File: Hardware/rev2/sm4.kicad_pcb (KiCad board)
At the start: 4 copper layers, 65 x 56 mm, 133 parts, among them J1 Motor1, J10 CAN bus, J2 Termination, J3 CAN bus, J4 Motor1, J5 I2C, J6 Power, J7 USB_C_Receptacle_USB2.0, J8 Conn_01x05_Male, J9 I2C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

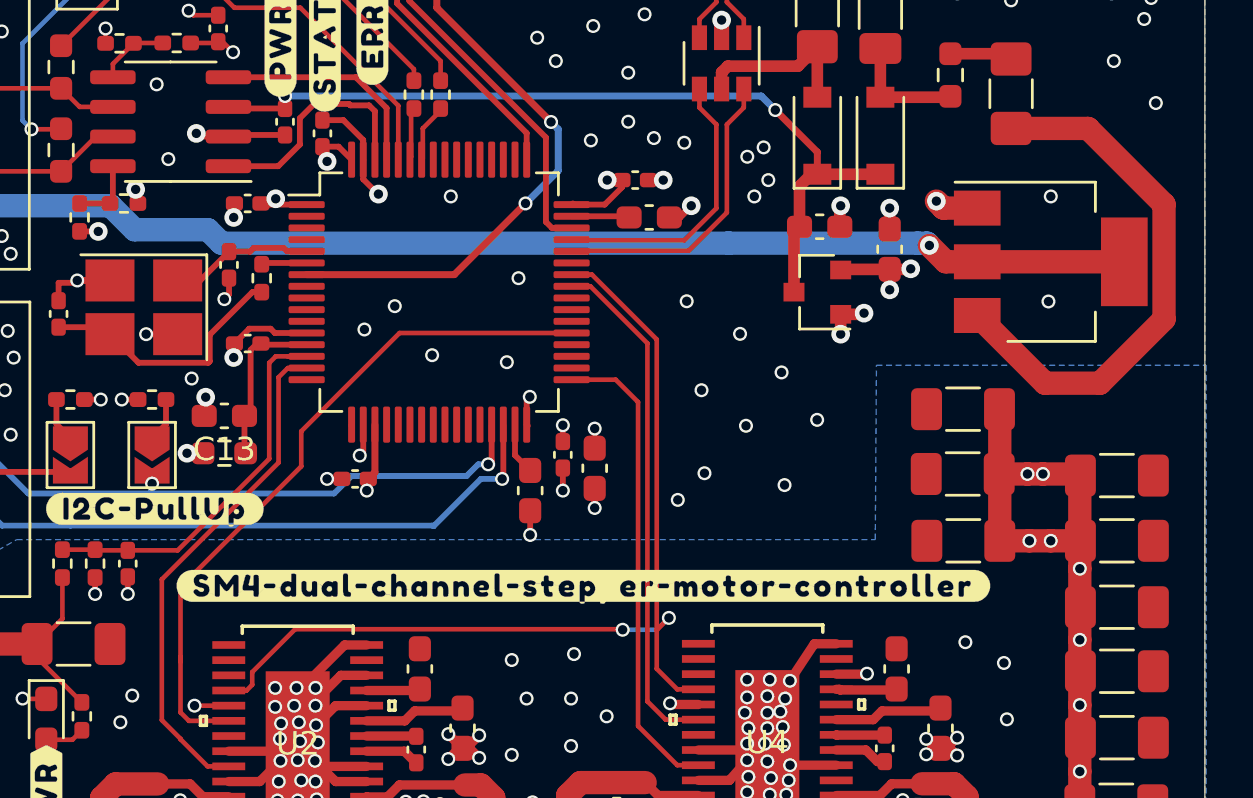
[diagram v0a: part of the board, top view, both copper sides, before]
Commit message: Start improving the second rev with feedback.
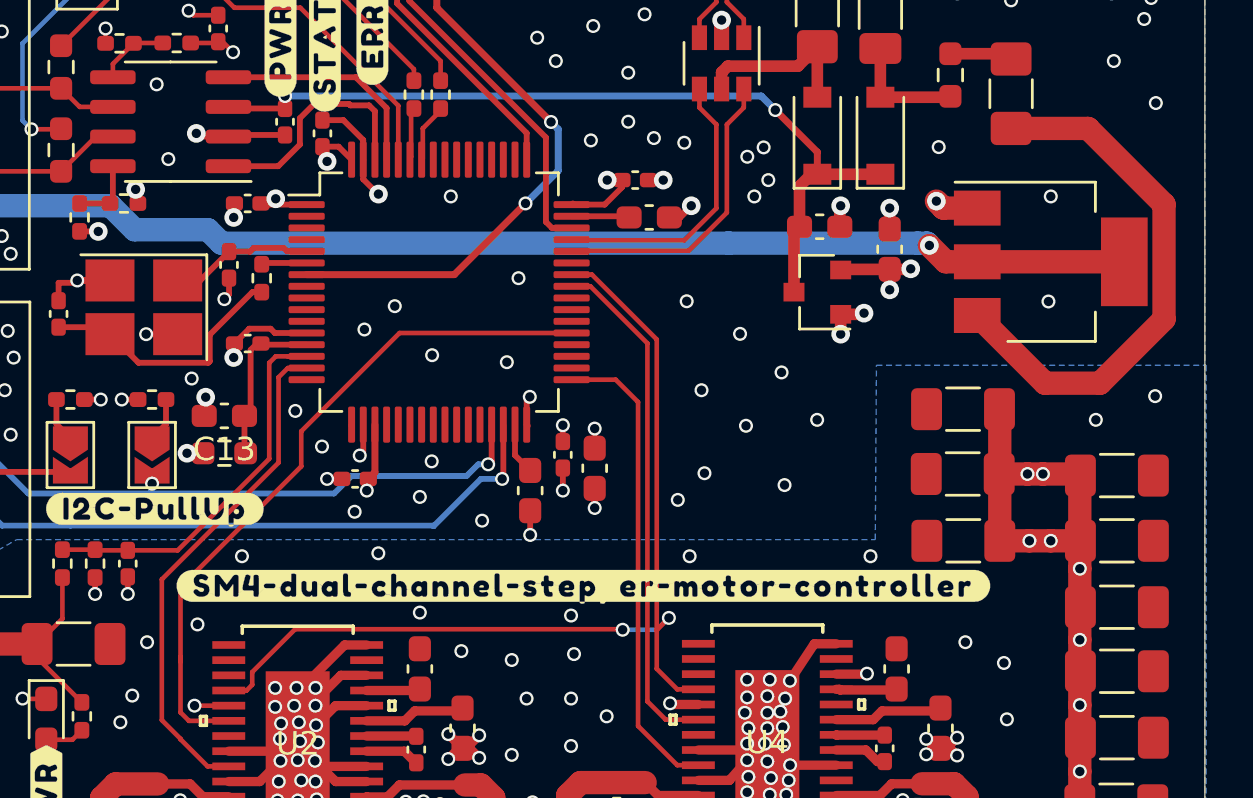
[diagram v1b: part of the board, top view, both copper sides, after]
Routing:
- net GND: vias 253 -> 271
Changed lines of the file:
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@@
     (thickness 1.6)
     (drawings 12)
-    (tracks 1001)
+    (tracks 1019)
     (zones 0)
     (modules 133)
@@
   (via (at 84.074 104.394) (size 0.6) (drill 0.4) (layers F.Cu B.Cu) (net 1))
   (via (at 92.583 104.013) (size 0.6) (drill 0.4) (layers F.Cu B.Cu) (net 1))
+  (via (at 71.374 80.772) (size 0.6) (drill 0.4) (layers F.Cu B.Cu) (net 1))
+  (via (at 68.58 81.407) (size 0.6) (drill 0.4) (layers F.Cu B.Cu) (net 1))
+  (via (at 67.183 78.613) (size 0.6) (drill 0.4) (layers F.Cu B.Cu) (net 1))
+  (via (at 66.04 77.089) (size 0.6) (drill 0.4) (layers F.Cu B.Cu) (net 1))
+  (via (at 74.041 81.788) (size 0.6) (drill 0.4) (layers F.Cu B.Cu) (net 1))
+  (via (at 71.882 79.248) (size 0.6) (drill 0.4) (layers F.Cu B.Cu) (net 1))
+  (via (at 73.152 87.376) (size 0.6) (drill 0.4) (layers F.Cu B.Cu) (net 1))
+  (via (at 71.374 85.725) (size 0.6) (drill 0.4) (layers F.Cu B.Cu) (net 1))
+  (via (at 77.851 85.852) (size 0.6) (drill 0.4) (layers F.Cu B.Cu) (net 1))
+  (via (at 69.596 83.185) (size 0.6) (drill 0.4) (layers F.Cu B.Cu) (net 1))
+  (via (at 63.754 83.312) (size 0.6) (drill 0.4) (layers F.Cu B.Cu) (net 1))
+  (via (at 61.849 86.233) (size 0.6) (drill 0.4) (layers F.Cu B.Cu) (net 1))
+  (via (at 59.69 86.995) (size 0.6) (drill 0.4) (layers F.Cu B.Cu) (net 1))
+  (via (at 82.931 83.312) (size 0.6) (drill 0.4) (layers F.Cu B.Cu) (net 1))
+  (via (at 90.678 83.312) (size 0.6) (drill 0.4) (layers F.Cu B.Cu) (net 1))
+  (via (at 102.87 76.454) (size 0.6) (drill 0.4) (layers F.Cu B.Cu) (net 1))
+  (via (at 100.33 77.47) (size 0.6) (drill 0.4) (layers F.Cu B.Cu) (net 1))
+  (via (at 93.599 65.786) (size 0.6) (drill 0.4) (layers F.Cu B.Cu) (net 1))
   (segment (start 75.45 78.9875) (end 76.1 79.6375) (width 0.25) (layer F.Cu) (net 2))
   (segment (start 75.45 77.675) (end 75.45 78.9875) (width 0.25) (layer F.Cu) (net 2))

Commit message: Make some final touches to the rev2 hardware.
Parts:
- added J11: GPIO, Connector_PinHeader_1.27mm:PinHeader_2x05_P1.27mm_Vertical, F.Cu at (73.9, 82.3)
- added J12: ENC_SPI, Connector_PinHeader_1.27mm:PinHeader_2x05_P1.27mm_Vertical, F.Cu at (85.0, 80.4)
- added J13: ENC_INC, Connector_PinHeader_1.27mm:PinHeader_2x05_P1.27mm_Vertical, F.Cu at (88.3, 75.3)
- added REF**: TestPoint_Pad_D1.0mm, TestPoint:TestPoint_Pad_D1.0mm, F.Cu at (61.6, 83.4)
- added REF**: TestPoint_Pad_D1.0mm, TestPoint:TestPoint_Pad_D1.0mm, F.Cu at (81.5, 90.3)
- added REF**: TestPoint_Pad_D1.0mm, TestPoint:TestPoint_Pad_D1.0mm, F.Cu at (79.9, 83.2)
- added REF**: TestPoint_Pad_D1.0mm, TestPoint:TestPoint_Pad_D1.0mm, F.Cu at (81.9, 83.2)
- added REF**: TestPoint_Pad_D1.0mm, TestPoint:TestPoint_Pad_D1.0mm, F.Cu at (81.3, 91.8)
- added REF**: TestPoint_Pad_D1.0mm, TestPoint:TestPoint_Pad_D1.0mm, F.Cu at (61.1, 91.6)
- J7: footprint Connector_USB:USB_C_Receptacle_GCT_USB4085 -> Connector_USB:USB_C_Receptacle_XKB_U262-16XN-4BVC11; moved to F.Cu
- R1, R2, R3, R5: footprint Resistor_SMD:R_0603_1608Metric_Pad0.98x0.95mm_HandSolder -> Resistor_SMD:R_1206_3216Metric_Pad1.30x1.75mm_HandSolder
- moved R23 11.0 mm to (82.4, 58.8), turned to 90 degrees
- moved J7 4.42 mm to (84.2, 52.7), turned to 180 degrees
- moved R22 4.14 mm to (86.2, 58.9), turned to 90 degrees
- moved C18 1.25 mm to (67.4, 79.8)
- moved ? 1.02 mm to (60.8, 85.6)
- moved R2 0.54 mm to (72.5, 96.4)
- moved R5 0.38 mm to (92.9, 96.3)
- moved R1 0.36 mm to (59.6, 96.3)
- moved R3 0.33 mm to (79.5, 96.1)
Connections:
- net MODE2 renamed Net-(U1-Pad43)
- U1 pad 14: VBAT -> ENC2A
- U1 pad 15: DIR1 -> ENC2B
- U1 pad 16: Net-(U1-Pad16) -> ENC2I
- U1 pad 17: MODE1 -> VBAT
- U1 pad 20: Net-(U1-Pad20) -> DIR1
- U1 pad 21: Net-(U1-Pad21) -> SCK1
- U1 pad 22: Net-(U1-Pad22) -> MISO1
- U1 pad 23: Net-(U1-Pad23) -> MOSI1
- U1 pad 24: Net-(U1-Pad24) -> GPIO1
- U1 pad 25: Net-(U1-Pad25) -> GPIO2
- U1 pad 26: Net-(U1-Pad26) -> GPIO3
- U1 pad 27: Net-(U1-Pad27) -> GPIO4
- U1 pad 28: Net-(U1-Pad28) -> GPIO5
- U1 pad 33: DIR2 -> Net-(U1-Pad33)
- U1 pad 34: Net-(U1-Pad34) -> SCK2
- U1 pad 35: Net-(U1-Pad35) -> MISO2
- U1 pad 36: Net-(U1-Pad36) -> MOSI2
- U1 pad 38: Net-(U1-Pad38) -> CS1
- U1 pad 39: Net-(U1-Pad39) -> CS2
- U1 pad 40: Net-(U1-Pad40) -> DIR2
- U1 pad 50: Net-(U1-Pad50) -> ENC1A
- U1 pad 55: Net-(U1-Pad55) -> ENC1B
- U1 pad 56: Net-(U1-Pad56) -> ENC1I
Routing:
- net ENC2A: track 0.00 -> 44.4 mm, vias 0 -> 1
- net ENC2B: track 0.00 -> 40.6 mm, vias 0 -> 1
- net ENC2I: track 0.00 -> 36.7 mm, vias 0 -> 1
- net ENC1I: track 0.00 -> 25.7 mm, vias 0 -> 1
- net +5V: track 36.0 -> 59.9 mm, vias 2 -> 3
- net ENC1B: track 0.00 -> 23.9 mm, vias 0 -> 1
- net ENC1A: track 0.00 -> 21.4 mm, vias 0 -> 1
- net SCK2: track 0.00 -> 21.4 mm, vias 0 -> 1
- net SCK1: track 0.00 -> 21.2 mm, vias 0 -> 1
- net MISO1: track 0.00 -> 20.9 mm, vias 0 -> 1
- net Net-(F2-Pad2): track 11.1 -> 31.7 mm, vias 0 -> 2
- net MOSI1: track 0.00 -> 19.1 mm, vias 0 -> 1
- net MISO2: track 0.00 -> 18.8 mm, vias 0 -> 1
- net +3V3: track 29.2 -> 47.0 mm
- net MOSI2: track 0.00 -> 15.7 mm, vias 0 -> 1
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
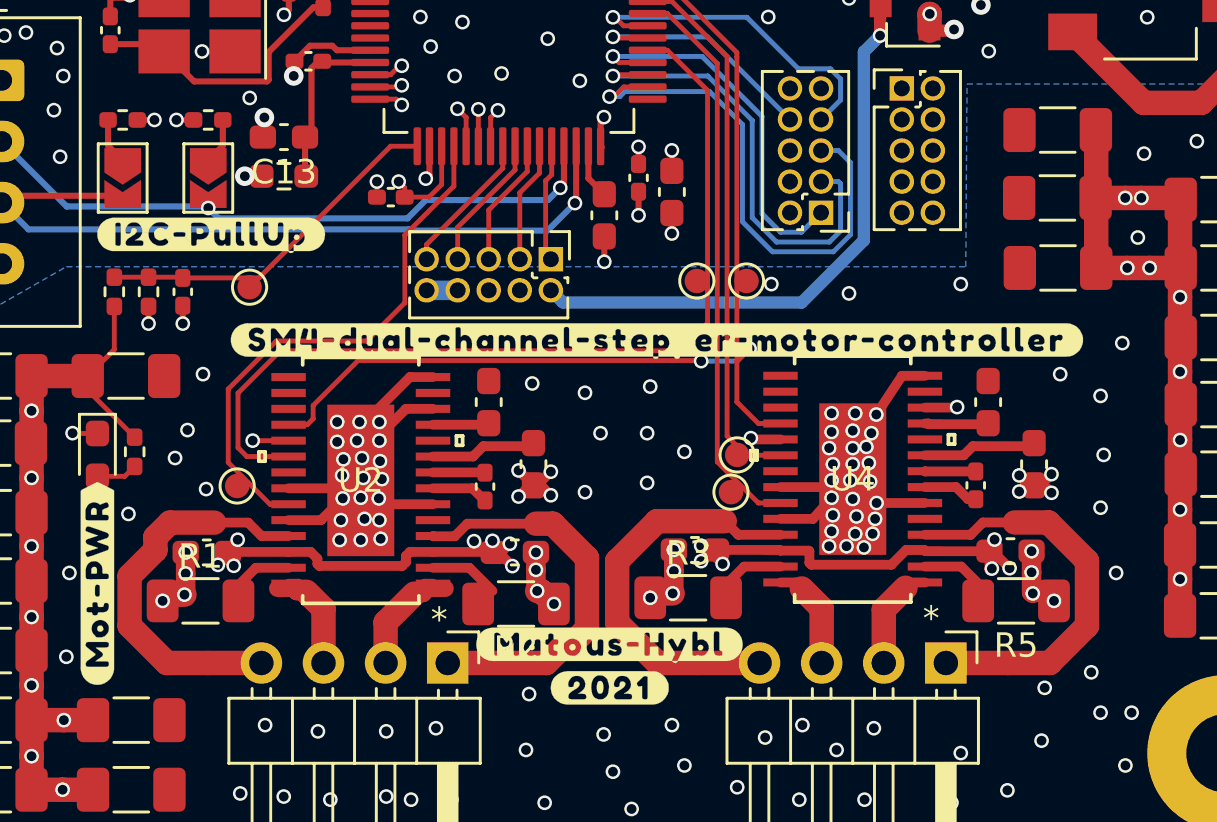
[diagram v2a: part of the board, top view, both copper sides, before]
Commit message: Implement more of the encoder model. Make some final adjustments to rev2 board and order it.
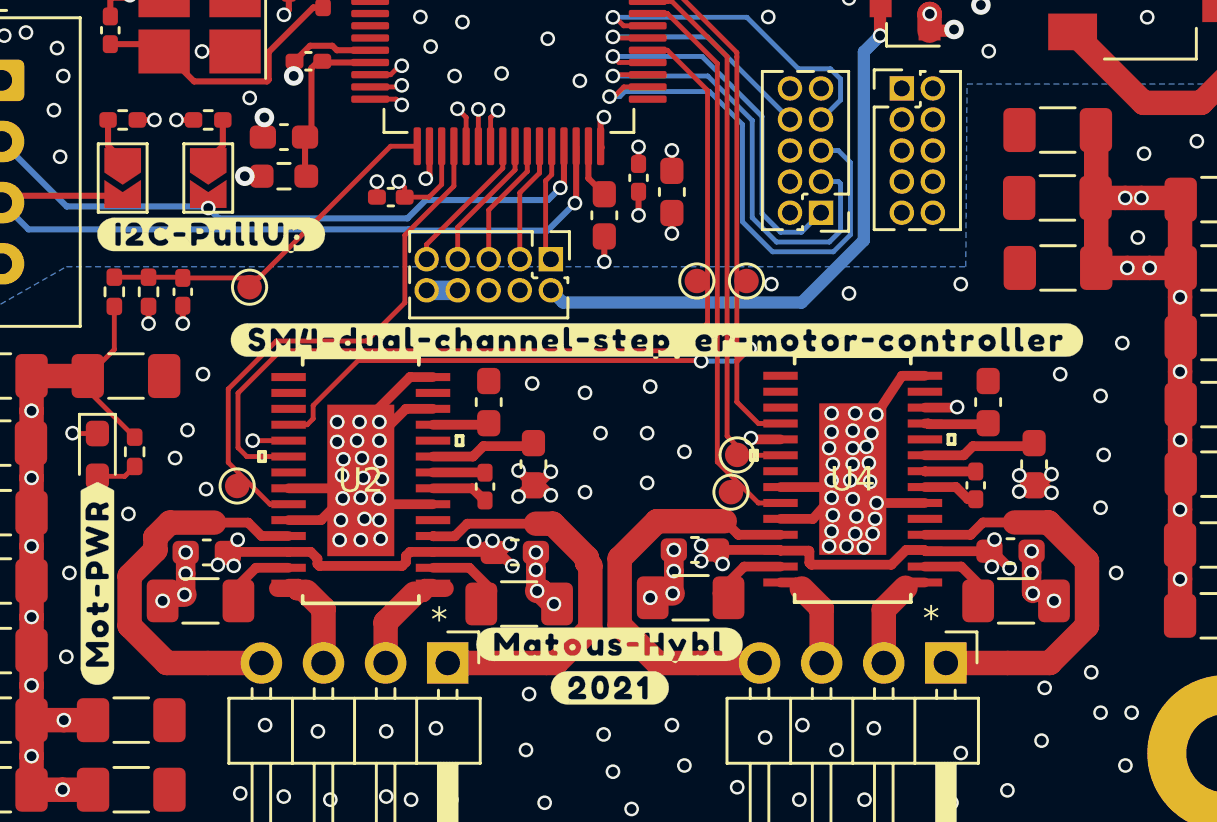
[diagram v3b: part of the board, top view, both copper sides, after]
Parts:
- moved R2 0.13 mm to (72.6, 96.4)
- moved R3 0.10 mm to (79.6, 96.1)
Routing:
- net VS1: track 100.8 -> 100.0 mm
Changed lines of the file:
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@@
     (thickness 1.6)
     (drawings 12)
-    (tracks 1247)
+    (tracks 1246)
     (zones 0)
     (modules 142)
@@
     (tags "resistor handsolder")
     (attr smd)
-    (fp_text reference R5 (at 0 -1.82) (layer F.SilkS)
+    (fp_text reference R5 (at 0 -1.82) (layer Cmts.User)
       (effects (font (size 1 1) (thickness 0.15)))
     )
@@
     (fp_line (start 2.45 -1.12) (end 2.45 1.12) (layer F.CrtYd) (width 0.05))
     (fp_line (start 2.45 1.12) (end -2.45 1.12) (layer F.CrtYd) (width 0.05))
-    (pad 2 smd roundrect (at 1.55 0 180) (size 1.3 1.75) (layers F.Cu F.Paste F.Mask) (roundrect_rratio 0.192308)
+    (pad 2 smd roundrect (at 1.55 0 180) (size 1.3 1.75) (layers F.Cu F.Paste F.Mask) (roundrect_rratio 0.1923076923076923)
       (net 90 BRB2))
-    (pad 1 smd roundrect (at -1.55 0 180) (size 1.3 1.75) (layers F.Cu F.Paste F.Mask) (roundrect_rratio 0.192308)
+    (pad 1 smd roundrect (at -1.55 0 180) (size 1.3 1.75) (layers F.Cu F.Paste F.Mask) (roundrect_rratio 0.1923076923076923)
       (net 1 GND))
     (model ${KISYS3DMOD}/Resistor_SMD.3dshapes/R_1206_3216Metric.wrl
@@
   )
   (module Resistor_SMD:R_1206_3216Metric_Pad1.30x1.75mm_HandSolder (layer F.Cu)
-    (at 79.528 96.139)
+    (at 79.629 96.139)
     (descr "Resistor SMD 1206 (3216 Metric), square (rectangular) end terminal, IPC_7351 nominal with elongated pad for handsoldering. (Body size source: IPC-SM-782 page 72, https://www.pcb-3d.com/wordpress/wp-content/uploads/ipc-sm-782a_amendment_1_and_2.pdf), generated with kicad-footprint-generator")
     (tags "resistor handsolder")
     (attr smd)
-    (fp_text reference R3 (at 0 -1.82) (layer F.SilkS)
+    (fp_text reference R3 (at 0 -1.82) (layer Cmts.User)
       (effects (font (size 1 1) (thickness 0.15)))
     )
@@
     (fp_line (start 2.45 -1.12) (end 2.45 1.12) (layer F.CrtYd) (width 0.05))
     (fp_line (start 2.45 1.12) (end -2.45 1.12) (layer F.CrtYd) (width 0.05))
-    (pad 2 smd roundrect (at 1.55 0) (size 1.3 1.75) (layers F.Cu F.Paste F.Mask) (roundrect_rratio 0.192308)
+    (pad 2 smd roundrect (at 1.55 0) (size 1.3 1.75) (layers F.Cu F.Paste F.Mask) (roundrect_rratio 0.1923076923076923)
       (net 89 BRA2))
-    (pad 1 smd roundrect (at -1.55 0) (size 1.3 1.75) (layers F.Cu F.Paste F.Mask) (roundrect_rratio 0.192308)
+    (pad 1 smd roundrect (at -1.55 0) (size 1.3 1.75) (layers F.Cu F.Paste F.Mask) (roundrect_rratio 0.1923076923076923)
       (net 1 GND))
     (model ${KISYS3DMOD}/Resistor_SMD.3dshapes/R_1206_3216Metric.wrl
@@
   )
   (module Resistor_SMD:R_1206_3216Metric_Pad1.30x1.75mm_HandSolder (layer F.Cu)
-    (at 72.491 96.393 180)
+    (at 72.618 96.393 180)
     (descr "Resistor SMD 1206 (3216 Metric), square (rectangular) end terminal, IPC_7351 nominal with elongated pad for handsoldering. (Body size source: IPC-SM-782 page 72, https://www.pcb-3d.com/wordpress/wp-content/uploads/ipc-sm-782a_amendment_1_and_2.pdf), generated with kicad-footprint-generator")
     (tags "resistor handsolder")
     (attr smd)
-    (fp_text reference R2 (at 0 -1.82) (layer F.SilkS)
+    (fp_text reference R2 (at 0 -1.82) (layer Cmts.User)
       (effects (font (size 1 1) (thickness 0.15)))
     )
@@
     (fp_line (start 2.45 -1.12) (end 2.45 1.12) (layer F.CrtYd) (width 0.05))
     (fp_line (start 2.45 1.12) (end -2.45 1.12) (layer F.CrtYd) (width 0.05))
-    (pad 2 smd roundrect (at 1.55 0 180) (size 1.3 1.75) (layers F.Cu F.Paste F.Mask) (roundrect_rratio 0.192308)
+    (pad 2 smd roundrect (at 1.55 0 180) (size 1.3 1.75) (layers F.Cu F.Paste F.Mask) (roundrect_rratio 0.1923076923076923)
       (net 58 BRB1))
-    (pad 1 smd roundrect (at -1.55 0 180) (size 1.3 1.75) (layers F.Cu F.Paste F.Mask) (roundrect_rratio 0.192308)
+    (pad 1 smd roundrect (at -1.55 0 180) (size 1.3 1.75) (layers F.Cu F.Paste F.Mask) (roundrect_rratio 0.1923076923076923)
       (net 1 GND))
     (model ${KISYS3DMOD}/Resistor_SMD.3dshapes/R_1206_3216Metric.wrl
@@
     (tags "resistor handsolder")
     (attr smd)
-    (fp_text reference R1 (at 0 -1.82) (layer F.SilkS)
+    (fp_text reference R1 (at 0 -1.82) (layer Cmts.User)
       (effects (font (size 1 1) (thickness 0.15)))
     )
@@
     (fp_line (start 2.45 -1.12) (end 2.45 1.12) (layer F.CrtYd) (width 0.05))
     (fp_line (start 2.45 1.12) (end -2.45 1.12) (layer F.CrtYd) (width 0.05))
-    (pad 2 smd roundrect (at 1.55 0) (size 1.3 1.75) (layers F.Cu F.Paste F.Mask) (roundrect_rratio 0.192308)
+    (pad 2 smd roundrect (at 1.55 0) (size 1.3 1.75) (layers F.Cu F.Paste F.Mask) (roundrect_rratio 0.1923076923076923)
       (net 57 BRA1))
-    (pad 1 smd roundrect (at -1.55 0) (size 1.3 1.75) (layers F.Cu F.Paste F.Mask) (roundrect_rratio 0.192308)
+    (pad 1 smd roundrect (at -1.55 0) (size 1.3 1.75) (layers F.Cu F.Paste F.Mask) (roundrect_rratio 0.1923076923076923)
       (net 1 GND))
     (model ${KISYS3DMOD}/Resistor_SMD.3dshapes/R_1206_3216Metric.wrl
@@
     (tags "capacitor handsolder")
     (attr smd)
-    (fp_text reference C13 (at 0 -1.43) (layer F.SilkS)
+    (fp_text reference C13 (at 0 -1.43) (layer Cmts.User)
       (effects (font (size 1 1) (thickness 0.15)))
     )
@@
   (segment (start 91.97656 94.234) (end 92.6725 94.92994) (width 0.4) (layer F.Cu) (net 4))
   (segment (start 91.8475 94.234) (end 91.97656 94.234) (width 0.4) (layer F.Cu) (net 4))
-  (via (at 91.948 94.9452) (size 0.6) (drill 0.4) (layers F.Cu B.Cu) (net 4))
-  (segment (start 91.8475 94.9971) (end 91.8972 95.0468) (width 0.4) (layer F.Cu) (net 4))
-  (segment (start 91.8475 94.234) (end 91.8475 94.9971) (width 0.4) (layer F.Cu) (net 4))
+  (via (at 91.948 94.869) (size 0.6) (drill 0.4) (layers F.Cu B.Cu) (net 4))
   (via (at 92.057206 93.75899) (size 0.6) (drill 0.4) (layers F.Cu B.Cu) (net 4))
   (segment (start 91.8475 93.968696) (end 92.057206 93.75899) (width 0.4) (layer F.Cu) (net 4))
@@
   (segment (start 73.99163 93.10979) (end 73.3044 93.10979) (width 1) (layer F.Cu) (net 53))
   (segment (start 75.39101 94.50917) (end 73.99163 93.10979) (width 1) (layer F.Cu) (net 53))
-  (segment (start 74.80533 97.99719) (end 75.39101 97.41151) (width 1) (layer F.Cu) (net 53))
-  (segment (start 74.54081 97.99719) (end 74.80533 97.99719) (width 1) (layer F.Cu) (net 53))
-  (segment (start 75.39101 97.41151) (end 75.39101 94.50917) (width 1) (layer F.Cu) (net 53))
-  (segment (start 73.732 98.806) (end 74.54081 97.99719) (width 1) (layer F.Cu) (net 53))
   (segment (start 69.6976 98.806) (end 73.732 98.806) (width 1) (layer F.Cu) (net 53))
+  (segment (start 74.12352 98.806) (end 73.732 98.806) (width 1) (layer F.Cu) (net 53))
+  (segment (start 75.52898 97.40054) (end 74.12352 98.806) (width 1) (layer F.Cu) (net 53))
+  (segment (start 75.52898 94.83298) (end 75.52898 97.40054) (width 1) (layer F.Cu) (net 53))
+  (segment (start 75.39101 94.69501) (end 75.52898 94.83298) (width 1) (layer F.Cu) (net 53))
+  (segment (start 75.39101 94.50917) (end 75.39101 94.69501) (width 1) (layer F.Cu) (net 53))
   (segment (start 69.09435 95.5634) (end 68.741 95.5634) (width 0.4) (layer F.Cu) (net 54))
   (segment (start 67.1576 97.1468) (end 68.3346 95.9698) (width 1) (layer F.Cu) (net 54))
@@
   (segment (start 81.026 93.00819) (end 81.580409 93.562599) (width 0.4) (layer F.Cu) (net 85))
   (segment (start 79.92766 98.806) (end 82.4484 98.806) (width 1) (layer F.Cu) (net 85))
-  (segment (start 76.62799 97.15751) (end 78.27648 98.806) (width 1) (layer F.Cu) (net 85))
   (segment (start 78.27648 98.806) (end 79.92766 98.806) (width 1) (layer F.Cu) (net 85))
-  (segment (start 76.62799 94.63507) (end 76.62799 97.15751) (width 1) (layer F.Cu) (net 85))
-  (segment (start 78.25487 93.00819) (end 76.62799 94.63507) (width 1) (layer F.Cu) (net 85))
   (segment (start 81.026 93.00819) (end 78.25487 93.00819) (width 1) (layer F.Cu) (net 85))
+  (segment (start 76.72899 97.25851) (end 78.27648 98.806) (width 1) (layer F.Cu) (net 85))
+  (segment (start 76.72899 94.53407) (end 76.72899 97.25851) (width 1) (layer F.Cu) (net 85))
+  (segment (start 78.25487 93.00819) (end 76.72899 94.53407) (width 1) (layer F.Cu) (net 85))
   (segment (start 83.9302 95.5126) (end 83.30565 95.5126) (width 0.4) (layer F.Cu) (net 86))
   (segment (start 84.9884 96.5708) (end 84.1756 95.758) (width 1) (layer F.Cu) (net 86))
